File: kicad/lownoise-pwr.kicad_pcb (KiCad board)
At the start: 2 copper layers, 78 x 36.9 mm, 27 parts, among them J1 Conn_01x02_Female, J2 Conn_01x02_Female, J3 Conn_01x02_Female, Q1 BD244C, U1 LM723_DIP14, U2 LM4040DBZ-4.1

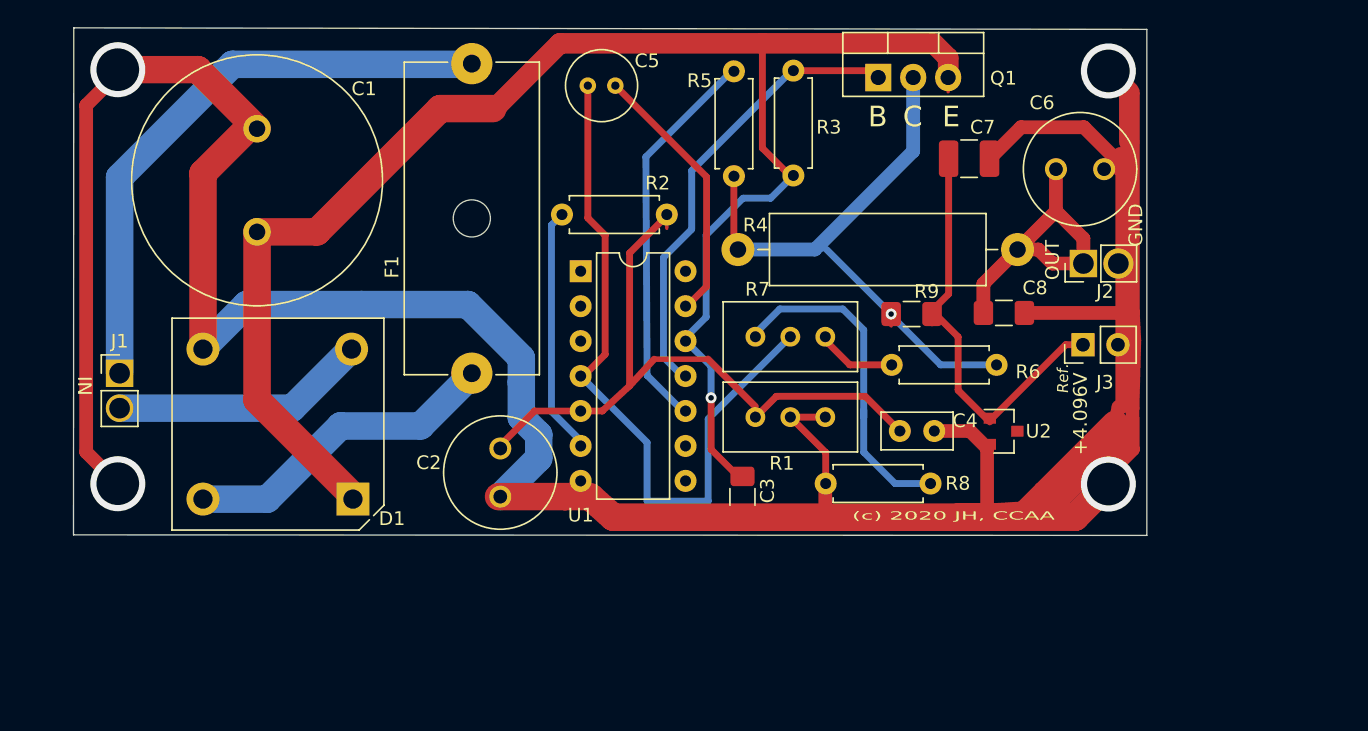
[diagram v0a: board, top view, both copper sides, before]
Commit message: Starts long way to screw-plugs
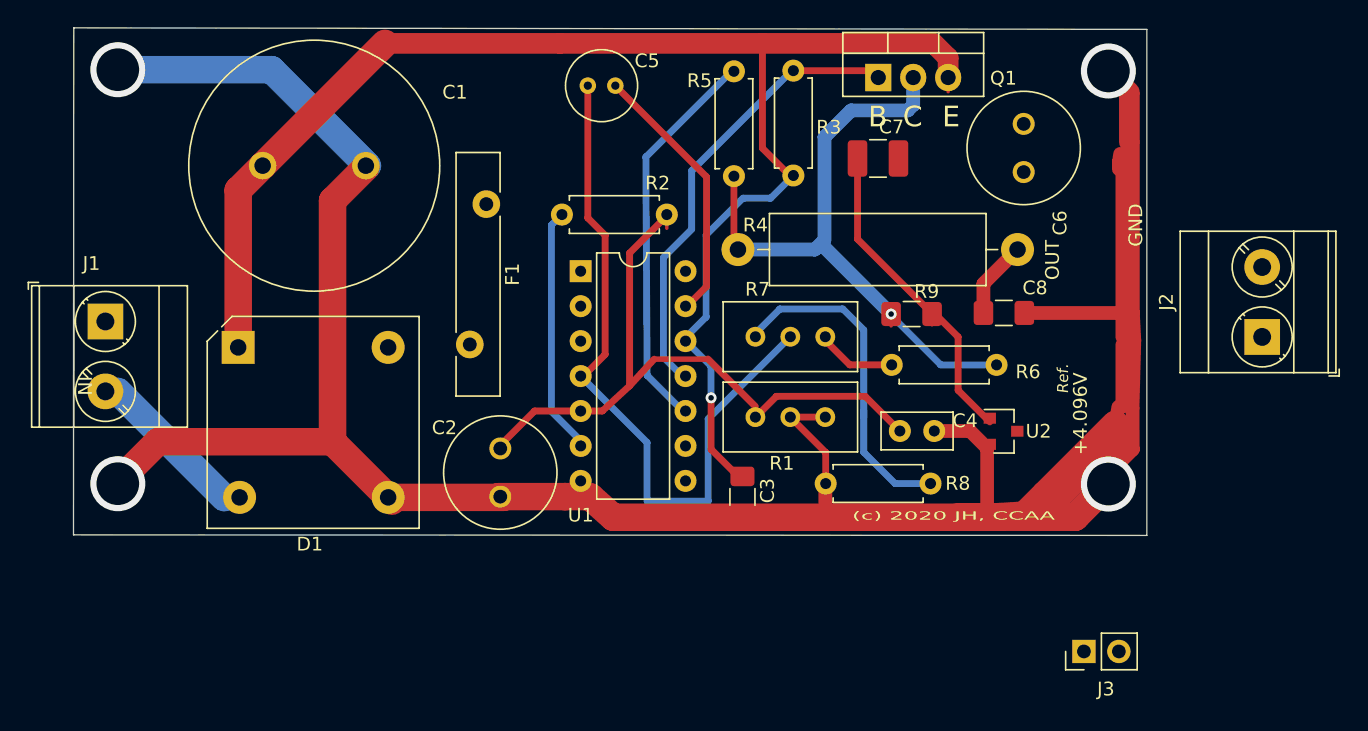
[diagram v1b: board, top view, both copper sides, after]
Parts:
- removed REF**: KiCad-Logo2_8mm_SilkScreen, Symbol:KiCad-Logo2_8mm_SilkScreen
- removed REF**: OSHW-Symbol_6.7x6mm_SilkScreen, Symbol:OSHW-Symbol_6.7x6mm_SilkScreen
- F1: footprint Fuse:Fuseholder_Cylinder-5x20mm_Schurter_0031_8201_Horizontal_Open -> Fuse:Fuse_Bourns_MF-RHT1000
- J1, J2: footprint Connector_PinHeader_2.54mm:PinHeader_1x02_P2.54mm_Vertical -> TerminalBlock_Phoenix:TerminalBlock_Phoenix_MKDS-3-2-5.08_1x02_P5.08mm_Horizontal
- moved J3 22.3 mm to (119.1, 105.2)
- moved J2 14.0 mm to (132.0, 82.3)
- moved D1 13.8 mm to (57.6, 83.1), turned to 0 degrees
- moved F1 10.3 mm to (75.6, 72.6)
- moved C7 6.62 mm to (104.1, 69.3)
- moved C1 4.83 mm to (59.4, 69.8), turned to 0 degrees
- moved J1 3.90 mm to (48.0, 81.2), turned to 270 degrees
- moved C6 2.36 mm to (114.7, 70.3), turned to 90 degrees
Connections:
- J2 pad 1: Net-(C6-Pad1) -> GND
- J2 pad 2: GND -> Net-(C6-Pad1)
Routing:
- net Net-(F1-Pad1): track 43.3 -> 0.19 mm
- net GND: track 268.3 -> 229.9 mm
- net Net-(D1-Pad4): track 23.4 -> 0.00 mm
- net Net-(C6-Pad1): track 23.1 -> 6.83 mm
- net Net-(C1-Pad1): track 122.4 -> 111.6 mm
- net Net-(C7-Pad1): track 31.6 -> 24.5 mm
- net Net-(D1-Pad2): track 18.6 -> 11.8 mm
- net Net-(Q1-Pad2): track 44.3 -> 46.6 mm

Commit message: Adds output screw-plugs, big transistor
R4 now vertical to gain space for screw-plugs
Input srew-plug not completely on PCB, soldered wires preferred
Adds 2nd via to solder polymer-fuse instead of glas fuseholder
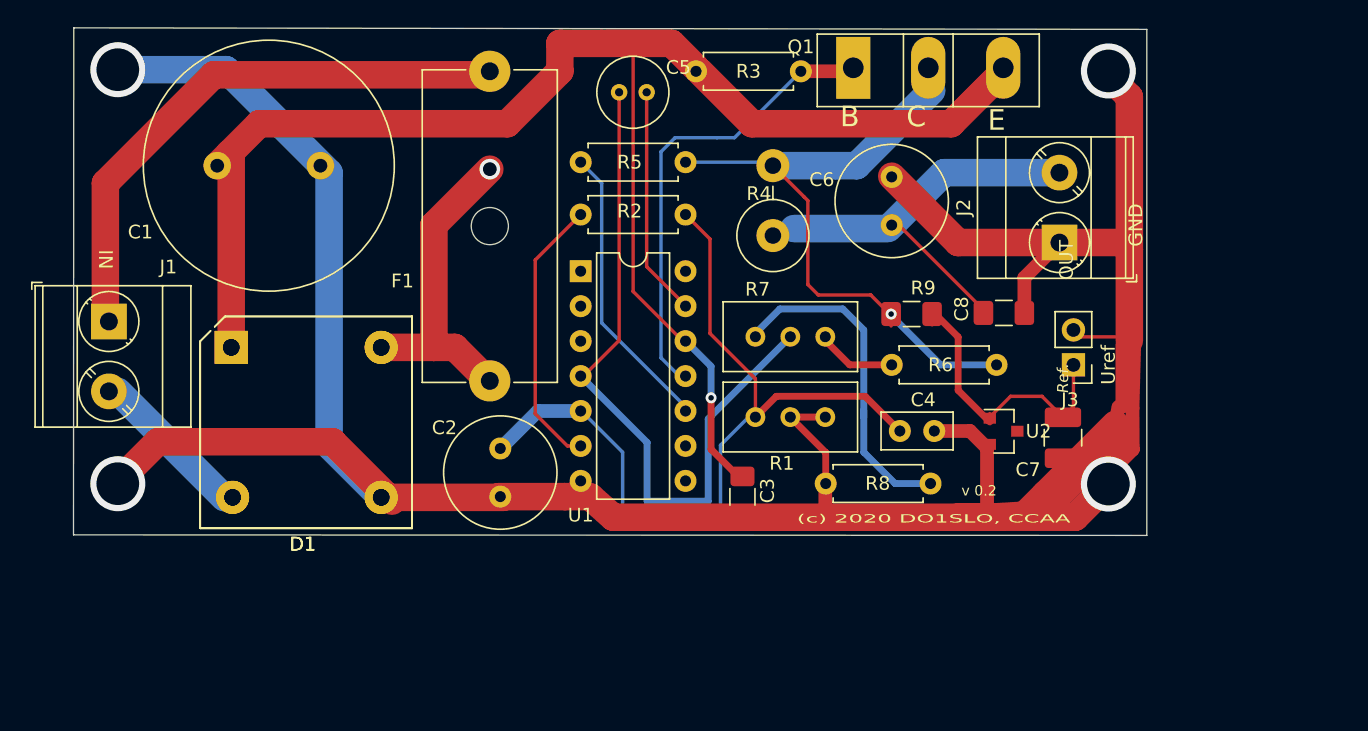
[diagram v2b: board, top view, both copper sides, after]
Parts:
- added D1: D_Bridge_+-AA, Diode_THT:Diode_Bridge_15.2x15.2x6.3mm_P10.9mm, F.Cu at (57.1, 83.1)
- F1: footprint Fuse:Fuse_Bourns_MF-RHT1000 -> Fuse:Fuseholder_Cylinder-5x20mm_Schurter_0031_8201_Horizontal_Open
- Q1: value BD244C -> BD244C / MJD6284; footprint Package_TO_SOT_THT:TO-220-3_Vertical -> Package_TO_SOT_THT:TO-247-3_Vertical
- R4: footprint Resistor_THT:R_Axial_DIN0516_L15.5mm_D5.0mm_P20.32mm_Horizontal -> Resistor_THT:R_Axial_DIN0516_L15.5mm_D5.0mm_P5.08mm_Vertical
- moved C7 24.3 mm to (117.6, 89.6), turned to 270 degrees
- moved J3 20.8 mm to (118.3, 84.3), turned to 180 degrees
- moved R4 17.8 mm to (96.5, 74.9), turned to 90 degrees
- moved J2 16.3 mm to (117.3, 75.4)
- moved C6 10.3 mm to (105.1, 74.2)
- moved F1 9.66 mm to (75.9, 63.0)
- moved R5 3.66 mm to (90.1, 69.6), turned to 180 degrees
- moved C1 3.30 mm to (56.1, 69.8)
- moved C5 2.33 mm to (85.3, 64.5)
- moved Q1 1.95 mm to (102.3, 62.7)
- moved R2 1.36 mm to (82.5, 73.4)
- moved R3 0.55 mm to (98.5, 63.0), turned to 180 degrees
- moved D1 0.51 mm to (57.1, 83.1)
- moved J1 0.25 mm to (48.2, 81.2)
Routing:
- net Net-(F1-Pad1): track 0.19 -> 41.7 mm
- net Net-(C6-Pad1): track 6.83 -> 30.6 mm
- net Net-(D1-Pad4): track 0.00 -> 23.2 mm, vias 0 -> 1
- net GND: track 229.9 -> 239.7 mm
- net Net-(C2-Pad1): track 50.8 -> 60.7 mm
- net Net-(R5-Pad2): track 28.9 -> 21.6 mm
- net Net-(C1-Pad1): track 111.6 -> 117.7 mm
- net Net-(C5-Pad2): track 19.5 -> 16.8 mm
- net Net-(R2-Pad1): track 18.0 -> 20.5 mm
- net Net-(C7-Pad1): track 24.5 -> 22.0 mm
- net Net-(Q1-Pad2): track 46.6 -> 47.2 mm
- net Net-(C5-Pad1): track 53.9 -> 53.3 mm
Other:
- board text added: "(c) 2020 DO1SLO, CCAA"
- board text added: "DO1SLO"
- board text added: "Uref"
- board text added: "v 0.2"
- board text removed: "(c) 2020 JH, CCAA"
- board text removed: "+4.096V"
